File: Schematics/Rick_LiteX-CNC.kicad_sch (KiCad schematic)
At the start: 0 parts

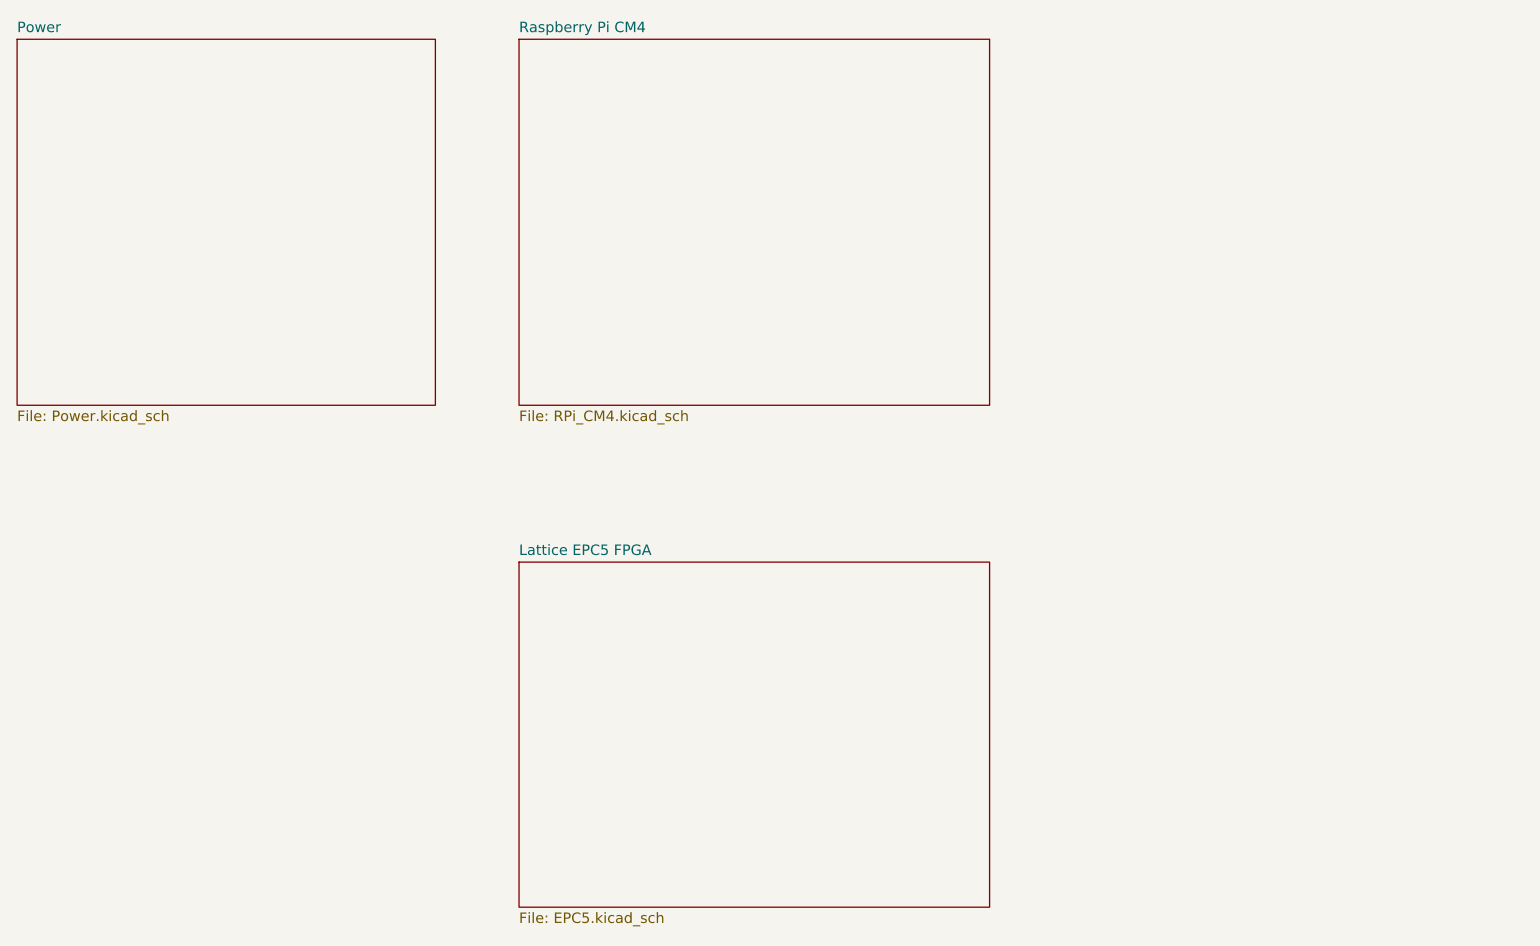
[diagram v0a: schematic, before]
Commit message: Need to order stencil
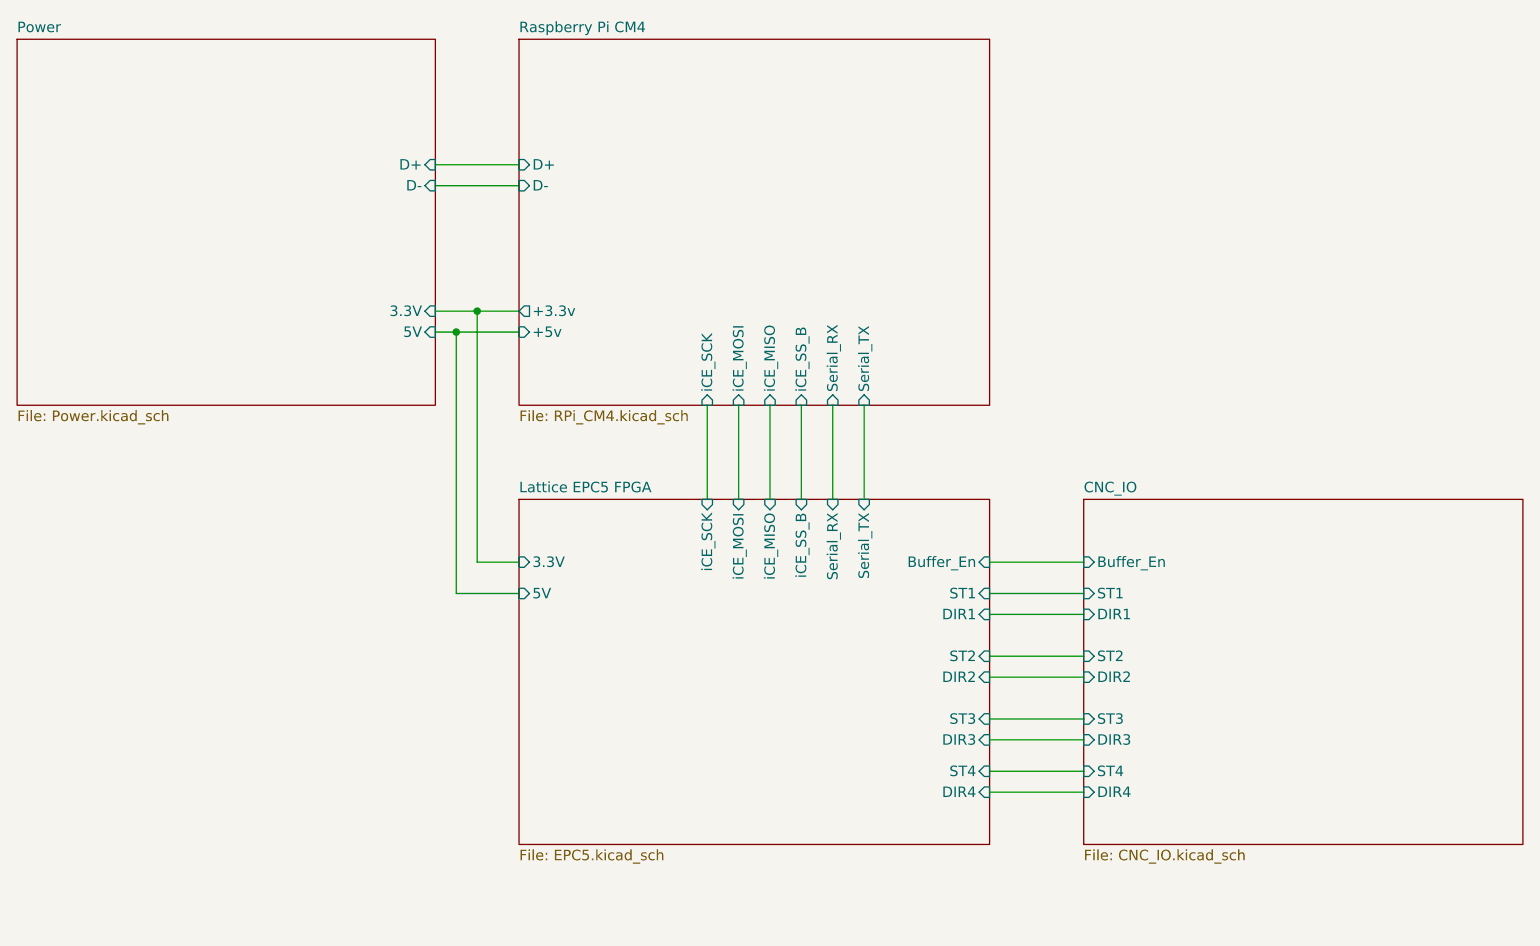
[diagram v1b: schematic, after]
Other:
- added sheet CNC_IO (CNC_IO.kicad_sch)
- sheet Lattice EPC5 FPGA ports: added 3.3V, 5V, Buffer_En, DIR1, DIR2, DIR3, DIR4, ST1, ST2, ST3, ST4, Serial_RX, Serial_TX, iCE_MISO, iCE_MOSI, iCE_SCK, iCE_SS_B; removed none
- sheet Power ports: added 3.3V, 5V, D+, D-; removed none
- sheet Raspberry Pi CM4 ports: added +3.3v, +5v, D+, D-, Serial_RX, Serial_TX, iCE_MISO, iCE_MOSI, iCE_SCK, iCE_SS_B; removed none
